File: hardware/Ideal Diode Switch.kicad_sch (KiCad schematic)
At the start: 41 parts, among them J9 Conn_01x12, Q10 SIR880BDP, Q11 SIR880BDP, Q12 SIR880BDP, Q5 SIR880BDP, Q6 SIR880BDP, Q7 SIR880BDP, Q8 SIR880BDP, Q9 SIR880BDP, U2 LM74810QDRRRQ1, U6 LM74810QDRRRQ1, U7 LM74810QDRRRQ1, U8 LM74810QDRRRQ1

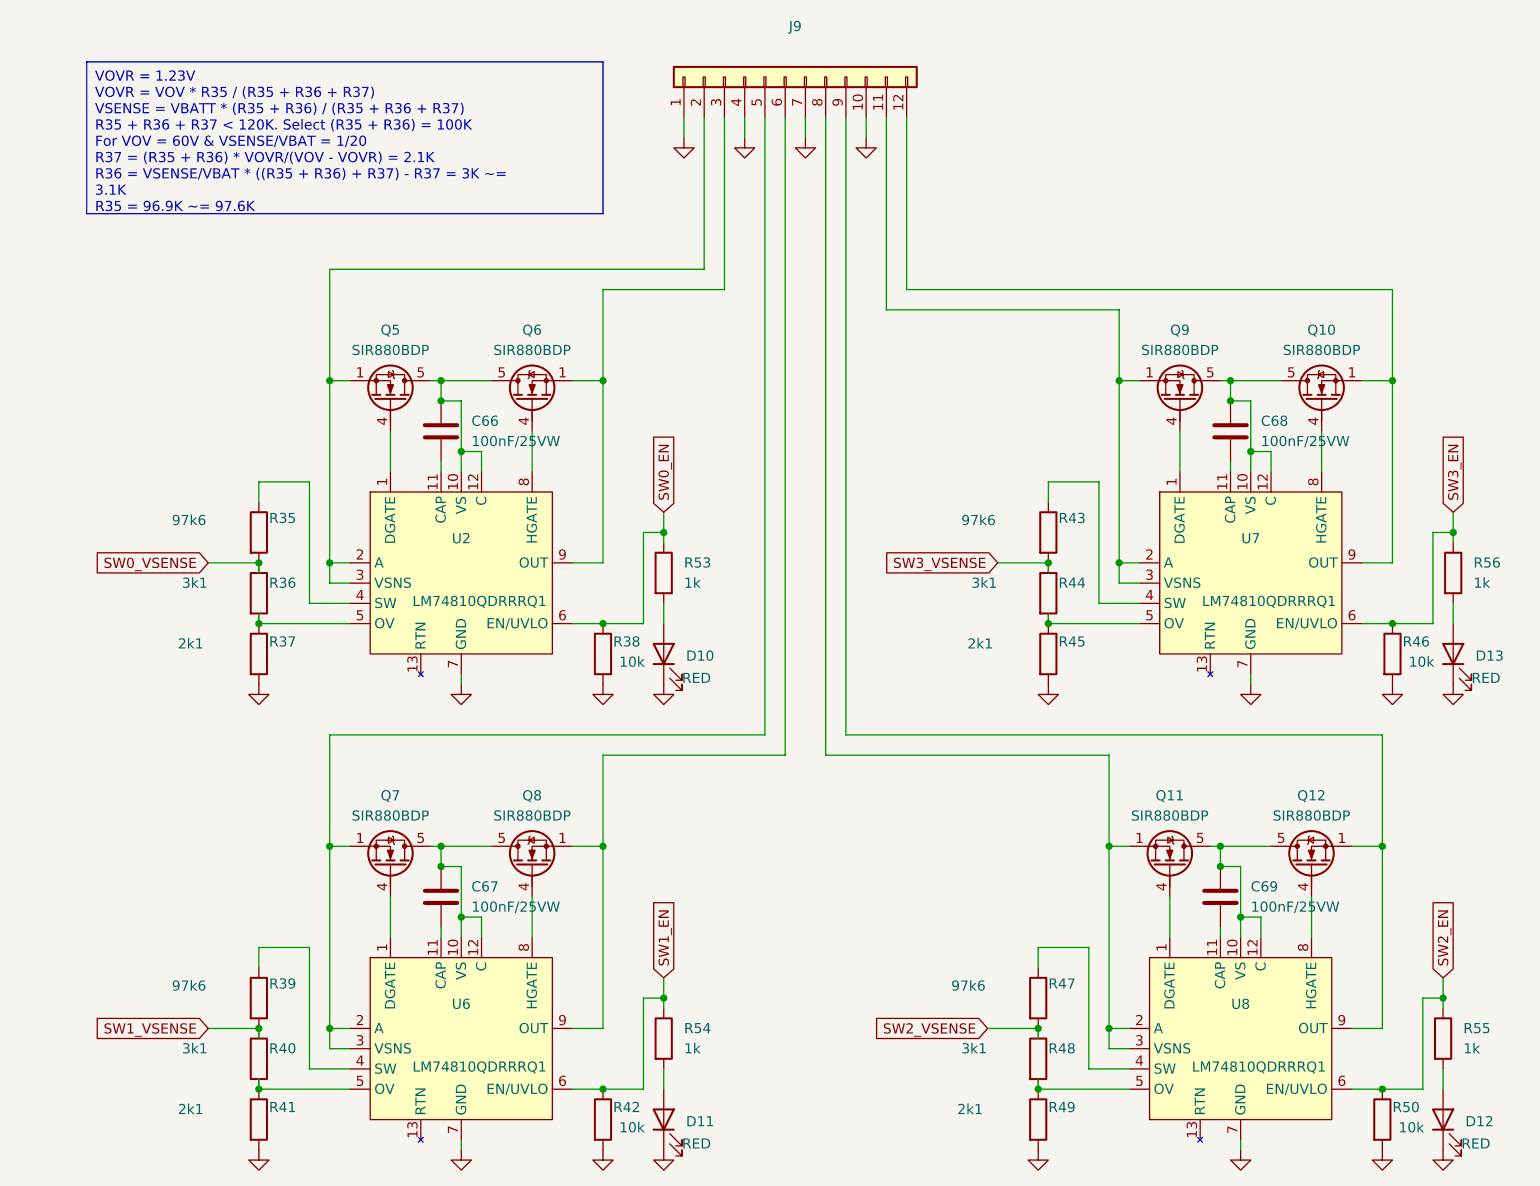
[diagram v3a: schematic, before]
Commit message: - Routed board with all fixable DRC errors and warnings fixed
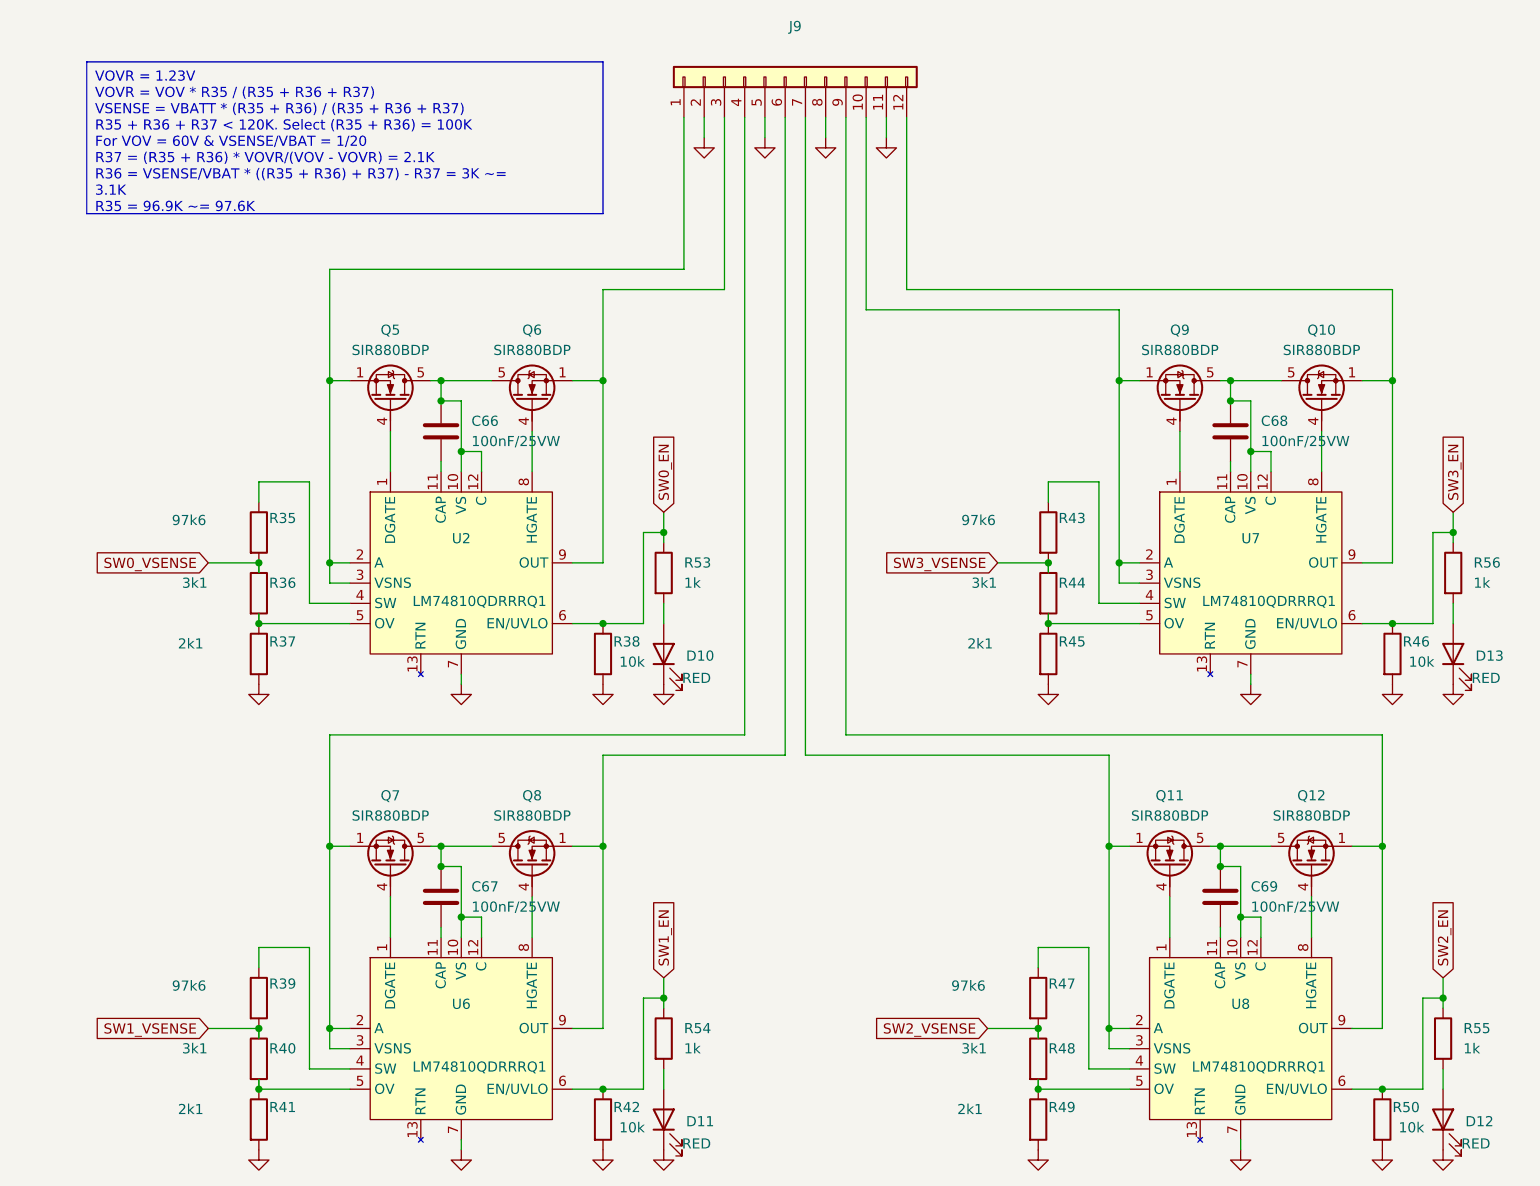
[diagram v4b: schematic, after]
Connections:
- net GND: now also J9.11 (Pin_11), J9.2 (Pin_2), J9.5 (Pin_5), J9.8 (Pin_8); no longer J9.1 (Pin_1), J9.10 (Pin_10), J9.4 (Pin_4), J9.7 (Pin_7)
- net at Q7.1 (S), Q7.2 (S), Q7.3 (S)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: now also J9.4 (Pin_4); no longer J9.5 (Pin_5)
- net at Q9.1 (S), Q9.2 (S), Q9.3 (S)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: now also J9.10 (Pin_10); no longer J9.11 (Pin_11)
- net at Q5.1 (S), Q5.2 (S), Q5.3 (S)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: now also J9.1 (Pin_1); no longer J9.2 (Pin_2)
- net at Q11.1 (S), Q11.2 (S), Q11.3 (S)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: now also J9.7 (Pin_7); no longer J9.8 (Pin_8)
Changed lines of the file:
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@@
 	(wire
 		(pts
-			(xy 123.19 27.94) (xy 123.19 52.07)
+			(xy 107.95 27.94) (xy 107.95 30.48)
 		)
 		(stroke
@@
 	(wire
 		(pts
+			(xy 113.03 27.94) (xy 113.03 107.95)
+		)
+		(stroke
+			(width 0)
+			(type default)
+		)
+	)
+	(wire
+		(pts
 			(xy 60.96 125.73) (xy 60.96 130.81)
 		)
@@
 	(wire
 		(pts
-			(xy 120.65 27.94) (xy 120.65 30.48)
+			(xy 166.37 63.5) (xy 168.91 63.5)
 		)
 		(stroke
@@
 	(wire
 		(pts
-			(xy 185.42 105.41) (xy 118.11 105.41)
+			(xy 118.11 27.94) (xy 118.11 105.41)
 		)
 		(stroke
@@
 	(wire
 		(pts
-			(xy 166.37 63.5) (xy 168.91 63.5)
+			(xy 120.65 52.07) (xy 152.4 52.07)
 		)
 		(stroke
@@
 	(wire
 		(pts
+			(xy 123.19 27.94) (xy 123.19 30.48)
+		)
+		(stroke
+			(width 0)
+			(type default)
+		)
+	)
+	(wire
+		(pts
 			(xy 69.85 128.27) (xy 69.85 130.81)
 		)
@@
 	(wire
 		(pts
+			(xy 113.03 107.95) (xy 151.13 107.95)
+		)
+		(stroke
+			(width 0)
+			(type default)
+		)
+	)
+	(wire
+		(pts
 			(xy 87.63 149.86) (xy 92.71 149.86)
 		)
@@
 	(wire
 		(pts
-			(xy 123.19 52.07) (xy 152.4 52.07)
+			(xy 97.79 27.94) (xy 97.79 46.99)
 		)
 		(stroke
@@
 	(wire
 		(pts
-			(xy 107.95 27.94) (xy 107.95 105.41)
+			(xy 44.45 90.17) (xy 44.45 91.44)
 		)
 		(stroke
@@
 	(wire
 		(pts
-			(xy 44.45 90.17) (xy 44.45 91.44)
+			(xy 186.69 91.44) (xy 191.77 91.44)
 		)
 		(stroke
@@
 	(wire
 		(pts
-			(xy 186.69 91.44) (xy 191.77 91.44)
+			(xy 100.33 27.94) (xy 100.33 30.48)
 		)
 		(stroke
@@
 	(wire
 		(pts
-			(xy 186.69 83.82) (xy 186.69 60.96)
+			(xy 105.41 27.94) (xy 105.41 105.41)
 		)
 		(stroke
@@
 	(wire
 		(pts
-			(xy 87.63 142.24) (xy 87.63 119.38)
+			(xy 186.69 83.82) (xy 186.69 60.96)
 		)
 		(stroke
@@
 	(wire
 		(pts
-			(xy 118.11 105.41) (xy 118.11 27.94)
+			(xy 87.63 142.24) (xy 87.63 119.38)
 		)
 		(stroke
@@
 	(wire
 		(pts
-			(xy 168.91 97.79) (xy 168.91 99.06)
-		)
-		(stroke
-			(width 0)
-			(type default)
-		)
-	)
-	(wire
-		(pts
-			(xy 67.31 60.96) (xy 67.31 63.5)
-		)
-		(stroke
-			(width 0)
-			(type default)
-		)
-	)
-	(wire
-		(pts
-			(xy 67.31 60.96) (xy 73.66 60.96)
+			(xy 120.65 27.94) (xy 120.65 52.07)
 		)
 		(stroke
@@
 	(wire
 		(pts
-			(xy 165.1 60.96) (xy 166.37 60.96)
+			(xy 168.91 97.79) (xy 168.91 99.06)
 		)
 		(stroke
@@
 	(wire
 		(pts
-			(xy 97.79 27.94) (xy 97.79 30.48)
+			(xy 67.31 60.96) (xy 67.31 63.5)
 		)
 		(stroke
@@
 	(wire
 		(pts
-			(xy 115.57 27.94) (xy 115.57 107.95)
+			(xy 67.31 60.96) (xy 73.66 60.96)
 		)
 		(stroke
@@
 	(wire
 		(pts
-			(xy 113.03 27.94) (xy 113.03 30.48)
+			(xy 165.1 60.96) (xy 166.37 60.96)
 		)
 		(stroke
@@
 	(wire
 		(pts
-			(xy 115.57 107.95) (xy 151.13 107.95)
-		)
-		(stroke
-			(width 0)
-			(type default)
-		)
-	)
-	(wire
-		(pts
 			(xy 67.31 129.54) (xy 67.31 130.81)
 		)
@@
 	(wire
 		(pts
-			(xy 105.41 27.94) (xy 105.41 30.48)
-		)
-		(stroke
-			(width 0)
-			(type default)
-		)
-	)
-	(wire
-		(pts
 			(xy 142.24 132.08) (xy 142.24 134.62)
 		)
@@
 	(wire
 		(pts
+			(xy 115.57 27.94) (xy 115.57 30.48)
+		)
+		(stroke
+			(width 0)
+			(type default)
+		)
+	)
+	(wire
+		(pts
 			(xy 152.4 60.96) (xy 152.4 83.82)
 		)
@@
 	(wire
 		(pts
-			(xy 53.34 46.99) (xy 100.33 46.99)
+			(xy 53.34 46.99) (xy 97.79 46.99)
 		)
 		(stroke
@@
 	(wire
 		(pts
-			(xy 100.33 27.94) (xy 100.33 46.99)
-		)
-		(stroke
-			(width 0)
-			(type default)
-		)
-	)
-	(wire
-		(pts
 			(xy 83.82 119.38) (xy 87.63 119.38)
 		)
@@
 	(wire
 		(pts
-			(xy 53.34 105.41) (xy 107.95 105.41)
+			(xy 53.34 105.41) (xy 105.41 105.41)
 		)
 		(stroke
@@
 	(wire
 		(pts
+			(xy 118.11 105.41) (xy 185.42 105.41)
+		)
+		(stroke
+			(width 0)
+			(type default)
+		)
+	)
+	(wire
+		(pts
 			(xy 66.04 119.38) (xy 67.31 119.38)
 		)
@@
 	(symbol
 		(lib_id "power:GND")
-		(at 97.79 30.48 0)
+		(at 100.33 30.48 0)
 		(unit 1)
 		(exclude_from_sim no)
@@
 		(fields_autoplaced yes)
 		(property "Reference" "#PWR089"
-			(at 97.79 36.83 0)
+			(at 100.33 36.83 0)
 			(effects
 				(font
@@
 		)
 		(property "Value" "GND"
-			(at 97.79 35.56 0)
+			(at 100.33 35.56 0)
 			(effects
 				(font
@@
 		)
 		(property "Footprint" ""
-			(at 97.79 30.48 0)
+			(at 100.33 30.48 0)
 			(effects
 				(font
@@
 		)
 		(property "Datasheet" ""
-			(at 97.79 30.48 0)
+			(at 100.33 30.48 0)
 			(effects
 				(font
@@
 		)
 		(property "Description" "Power symbol creates a global label with name \"GND\" , ground"
-			(at 97.79 30.48 0)
+			(at 100.33 30.48 0)
 			(effects
 				(font
@@
 	(symbol
 		(lib_id "power:GND")
-		(at 113.03 30.48 0)
+		(at 115.57 30.48 0)
 		(unit 1)
 		(exclude_from_sim no)
@@
 		(fields_autoplaced yes)
 		(property "Reference" "#PWR091"
-			(at 113.03 36.83 0)
+			(at 115.57 36.83 0)
 			(effects
 				(font
@@
 		)
 		(property "Value" "GND"
-			(at 113.03 35.56 0)
+			(at 115.57 35.56 0)
 			(effects
 				(font
@@
 		)
 		(property "Footprint" ""
-			(at 113.03 30.48 0)
+			(at 115.57 30.48 0)
 			(effects
 				(font
@@
 		)
 		(property "Datasheet" ""
-			(at 113.03 30.48 0)
+			(at 115.57 30.48 0)
 			(effects
 				(font
@@
 		)
 		(property "Description" "Power symbol creates a global label with name \"GND\" , ground"
-			(at 113.03 30.48 0)
+			(at 115.57 30.48 0)
 			(effects
 				(font
@@
 	(symbol
 		(lib_id "power:GND")
-		(at 120.65 30.48 0)
+		(at 123.19 30.48 0)
 		(unit 1)
 		(exclude_from_sim no)
@@
 		(fields_autoplaced yes)
 		(property "Reference" "#PWR092"
-			(at 120.65 36.83 0)
+			(at 123.19 36.83 0)
 			(effects
 				(font
@@
 		)
 		(property "Value" "GND"
-			(at 120.65 35.56 0)
+			(at 123.19 35.56 0)
 			(effects
 				(font
@@
 		)
 		(property "Footprint" ""
-			(at 120.65 30.48 0)
+			(at 123.19 30.48 0)
 			(effects
 				(font
@@
 		)
 		(property "Datasheet" ""
-			(at 120.65 30.48 0)
+			(at 123.19 30.48 0)
 			(effects
 				(font
@@
 		)
 		(property "Description" "Power symbol creates a global label with name \"GND\" , ground"
-			(at 120.65 30.48 0)
+			(at 123.19 30.48 0)
 			(effects
 				(font
@@
 	(symbol
 		(lib_id "power:GND")
-		(at 105.41 30.48 0)
+		(at 107.95 30.48 0)
 		(unit 1)
 		(exclude_from_sim no)
@@
 		(fields_autoplaced yes)
 		(property "Reference" "#PWR090"
-			(at 105.41 36.83 0)
+			(at 107.95 36.83 0)
 			(effects
 				(font
@@
 		)
 		(property "Value" "GND"
-			(at 105.41 35.56 0)
+			(at 107.95 35.56 0)
 			(effects
 				(font
@@
 		)
 		(property "Footprint" ""
-			(at 105.41 30.48 0)
+			(at 107.95 30.48 0)
 			(effects
 				(font
@@
 		)
 		(property "Datasheet" ""
-			(at 105.41 30.48 0)
+			(at 107.95 30.48 0)
 			(effects
 				(font
@@
 		)
 		(property "Description" "Power symbol creates a global label with name \"GND\" , ground"
-			(at 105.41 30.48 0)
+			(at 107.95 30.48 0)
 			(effects
 				(font

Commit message: Ready for trial submit to JLCPCB
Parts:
- added C70, C71, C72, C73: 100nF/100VW, Capacitor_SMD:C_1206_3216Metric, symbol Device:C
- added R59, R60, R61, R62: 0R, Resistor_SMD:R_0603_1608Metric, symbol Device:R
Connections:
- net GND: now also C70.2, C71.2, C72.2, C73.2
- net at Q8.1 (S), Q8.2 (S), Q8.3 (S)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: now also J9.7 (Pin_7); no longer J9.6 (Pin_6)
- net at C67.1, Q7.5 (D), Q7.6 (D)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: now also C71.1
- net at Q7.1 (S), Q7.2 (S), Q7.3 (S)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: now also J9.9 (Pin_9), R60.1; no longer J9.4 (Pin_4)
- net at R39.1, U6.4 (SW): now also R60.2
- net at Q5.1 (S), Q5.2 (S), Q5.3 (S)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: now also J9.12 (Pin_12), R59.1; no longer J9.1 (Pin_1)
- net at Q9.1 (S), Q9.2 (S), Q9.3 (S)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: now also J9.3 (Pin_3), R61.1; no longer J9.10 (Pin_10)
- net at Q10.1 (S), Q10.2 (S), Q10.3 (S)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: now also J9.1 (Pin_1); no longer J9.12 (Pin_12)
- net at Q6.1 (S), Q6.2 (S), Q6.3 (S)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: now also J9.10 (Pin_10); no longer J9.3 (Pin_3)
- net at Q11.1 (S), Q11.2 (S), Q11.3 (S)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: now also J9.6 (Pin_6), R62.1; no longer J9.7 (Pin_7)
- net at Q12.1 (S), Q12.2 (S), Q12.3 (S)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: now also J9.4 (Pin_4); no longer J9.9 (Pin_9)
- net at R47.1, U8.4 (SW): now also R62.2
- net at C66.1, Q5.5 (D), Q5.6 (D)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: now also C70.1
- net at C68.1, Q10.5 (D), Q10.6 (D)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: now also C73.1
- net at R43.1, U7.4 (SW): now also R61.2
- net at C69.1, Q11.5 (D), Q11.6 (D)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: now also C72.1
- net at R35.1, U2.4 (SW): now also R59.2
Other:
- moved on the sheet: J9

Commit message: * Added the JLCPCB Fabrication Plugin into KiCad and use this for the exports * Fixed problem detected with capacitor footprint for C42, C43, C44, C50, C51, C52
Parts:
- C66, C67, C68, C69: LCSC Part (none) -> C1590
- C70, C71, C72, C73: LCSC Part (none) -> C1945
- D10, D11, D12, D13: LCSC Part (none) -> C2286
- R35, R39, R43, R47: LCSC Part (none) -> C2907079
- R36, R40, R44, R48: LCSC Part (none) -> C2924132
- R37, R41, R45, R49: LCSC Part (none) -> C22902
- R38, R42, R46, R50: LCSC Part (none) -> C25804
- R53, R54, R55, R56: LCSC Part (none) -> C21190
